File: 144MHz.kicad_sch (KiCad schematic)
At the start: 45 parts, among them J4 BWSMA-KWE-Z001, U5 GRF5604, U6 SKYA21003

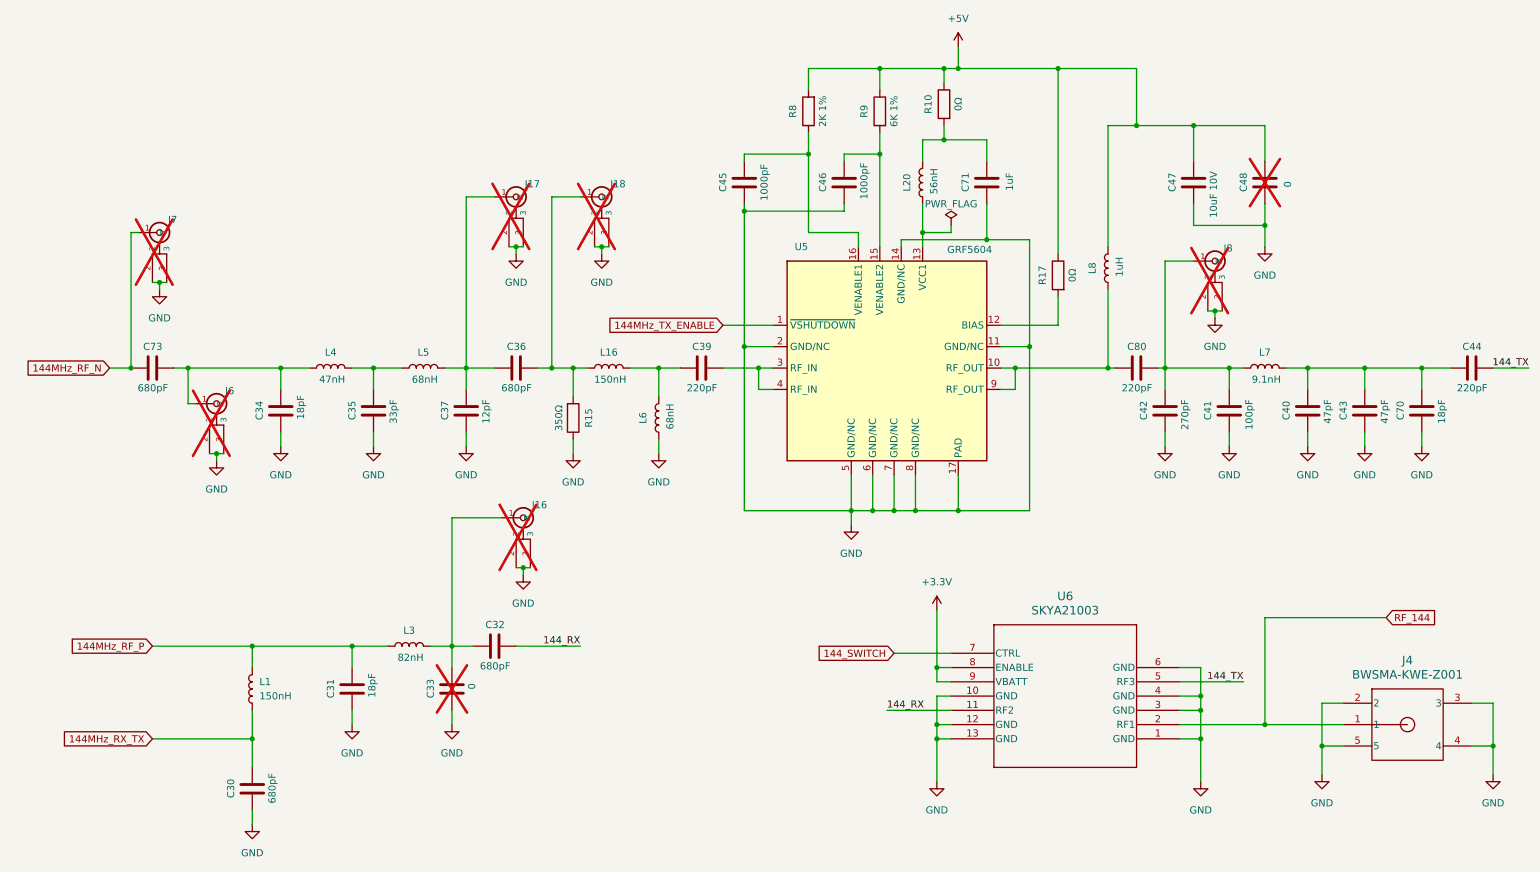
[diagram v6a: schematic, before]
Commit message: Reduce hole sizes and add more holes on PA
Meet spec requirements.

Signed-off-by: Corey Minyard <corey@minyard.net>
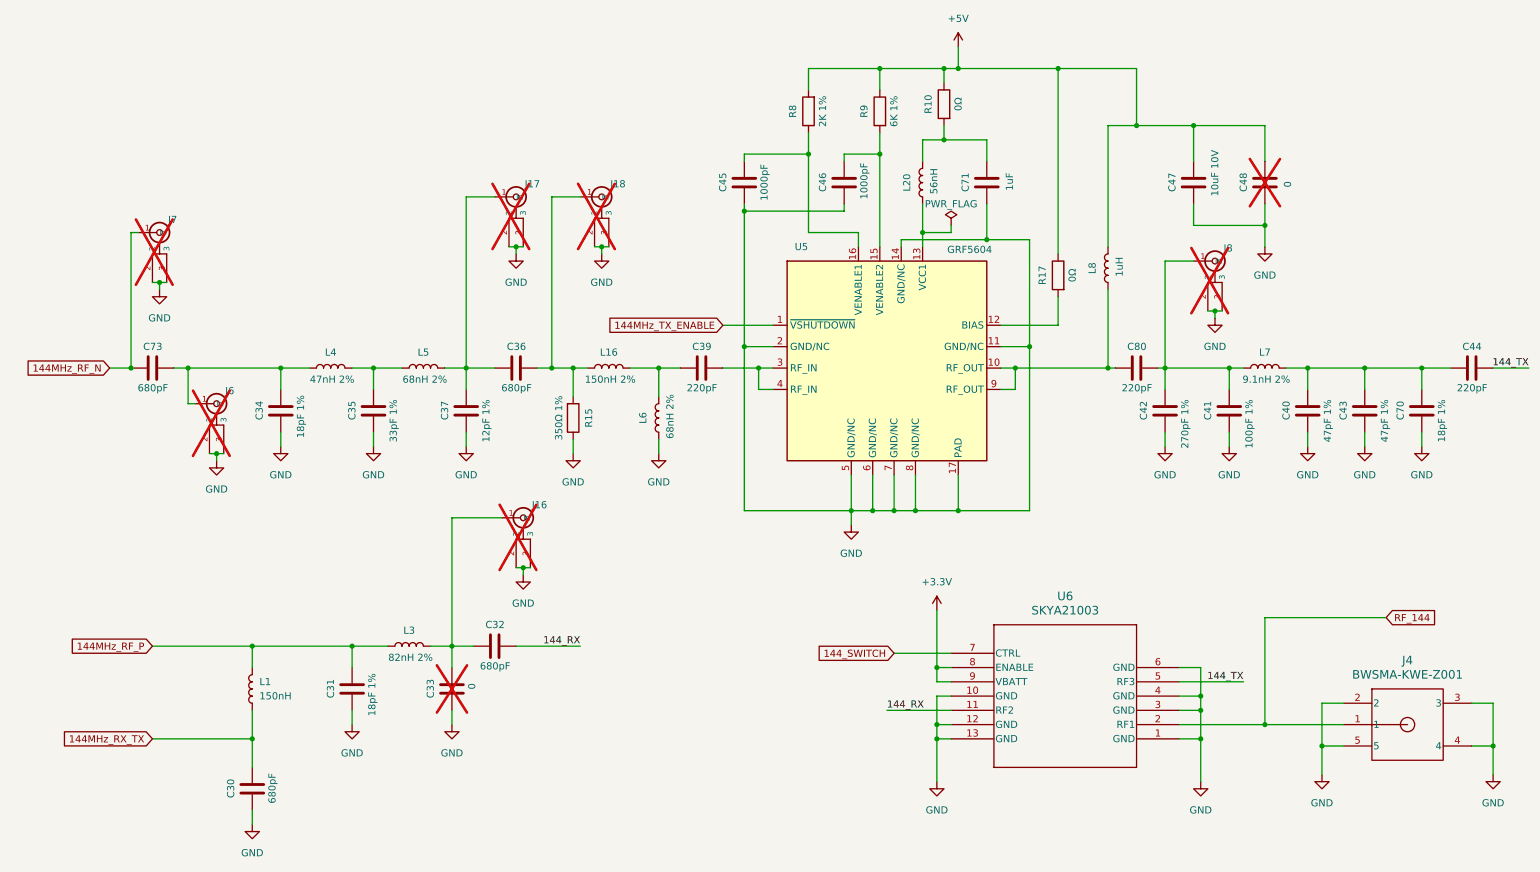
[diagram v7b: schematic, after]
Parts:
- C31, C34, C70: value 18pF -> 18pF 1%
- C35: value 33pF -> 33pF 1%
- C37: value 12pF -> 12pF 1%
- C40, C43: value 47pF -> 47pF 1%
- C41: value 100pF -> 100pF 1%
- C42: value 270pF -> 270pF 1%
- L16: value 150nH -> 150nH 2%
- L3: value 82nH -> 82nH 2%
- L4: value 47nH -> 47nH 2%
- L5, L6: value 68nH -> 68nH 2%
- L7: value 9.1nH -> 9.1nH 2%
- R15: value 350Ω -> 350Ω 1%
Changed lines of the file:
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@@
 			)
 		)
-		(property "Value" "68nH"
+		(property "Value" "68nH 2%"
 			(at 85.344 80.772 90)
 			(effects
@@
 		)
 		(property "Value" "10uF 10V"
-			(at 225.806 43.688 90)
+			(at 226.06 39.878 90)
 			(effects
 				(font
@@
 			)
 		)
-		(property "Value" "150nH"
+		(property "Value" "150nH 2%"
 			(at 118.364 80.772 90)
 			(effects
@@
 			)
 		)
-		(property "Value" "270pF"
+		(property "Value" "270pF 1%"
 			(at 220.726 84.328 90)
 			(effects
@@
 			)
 		)
-		(property "Value" "9.1nH"
+		(property "Value" "9.1nH 2%"
 			(at 235.204 80.772 90)
 			(effects
@@
 			)
 		)
-		(property "Value" "18pF"
+		(property "Value" "18pF 1%"
 			(at 63.246 83.566 90)
 			(effects
@@
 			)
 		)
-		(property "Value" "12pF"
+		(property "Value" "12pF 1%"
 			(at 96.266 84.328 90)
 			(effects
@@
 			)
 		)
-		(property "Value" "68nH"
+		(property "Value" "68nH 2%"
 			(at 129.032 87.376 90)
 			(effects
@@
 			)
 		)
-		(property "Value" "47pF"
+		(property "Value" "47pF 1%"
 			(at 256.286 84.328 90)
 			(effects
@@
 			)
 		)
-		(property "Value" "82nH"
+		(property "Value" "82nH 2%"
 			(at 82.804 130.302 90)
 			(effects
@@
 			)
 		)
-		(property "Value" "33pF"
+		(property "Value" "33pF 1%"
 			(at 79.756 84.328 90)
 			(effects
@@
 			)
 		)
-		(property "Value" "47nH"
+		(property "Value" "47nH 2%"
 			(at 68.834 80.772 90)
 			(effects
@@
 			)
 		)
-		(property "Value" "47pF"
+		(property "Value" "47pF 1%"
 			(at 246.126 84.328 90)
 			(effects
@@
 			)
 		)
-		(property "Value" "100pF"
+		(property "Value" "100pF 1%"
 			(at 232.156 84.328 90)
 			(effects
@@
 			)
 		)
-		(property "Value" "18pF"
+		(property "Value" "18pF 1%"
 			(at 75.946 133.096 90)
 			(effects
@@
 			)
 		)
-		(property "Value" "18pF"
+		(property "Value" "18pF 1%"
 			(at 266.446 84.328 90)
 			(effects
@@
 			)
 		)
-		(property "Value" "350Ω"
+		(property "Value" "350Ω 1%"
 			(at 109.22 87.63 90)
 			(effects

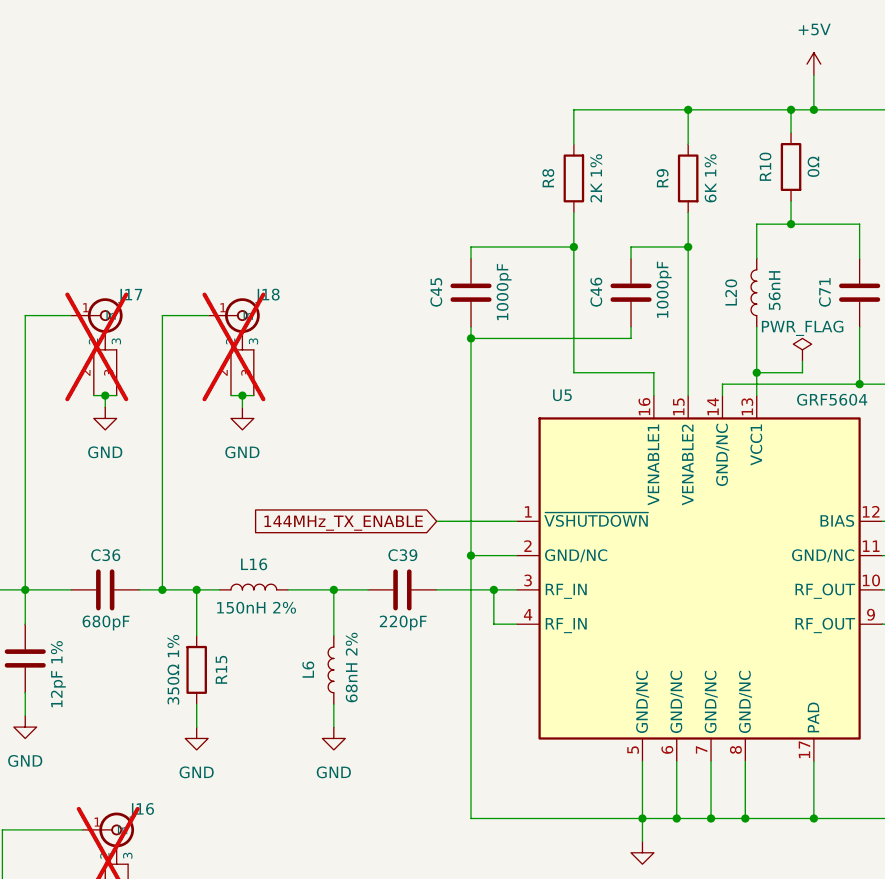
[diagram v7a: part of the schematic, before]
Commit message: Start working on BOM, fix supply indoctors
Signed-off-by: Corey Minyard <corey@minyard.net>
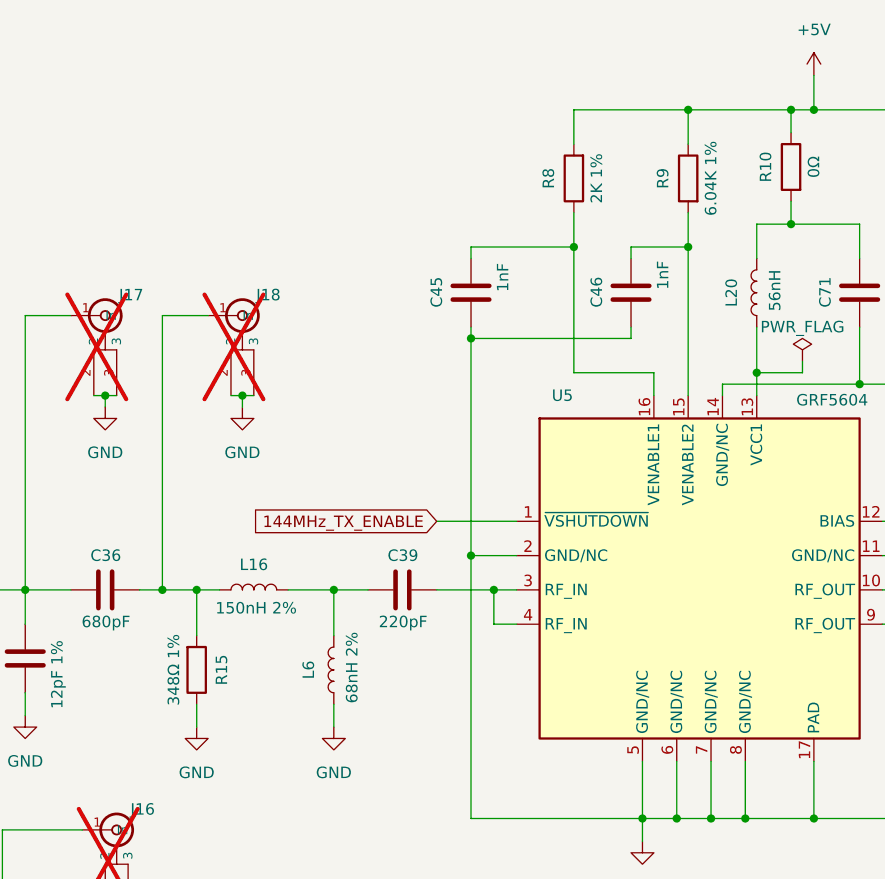
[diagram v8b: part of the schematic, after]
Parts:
- C45, C46: value 1000pF -> 1nF
- C47: footprint Capacitor_SMD:C_0805_2012Metric_Pad1.18x1.45mm_HandSolder -> Capacitor_SMD:C_1206_3216Metric_Pad1.33x1.80mm_HandSolder
- C71: footprint Capacitor_SMD:C_0402_1005Metric_Pad0.74x0.62mm_HandSolder -> Capacitor_SMD:C_0603_1608Metric_Pad1.08x0.95mm_HandSolder
- L8: footprint Inductor_SMD:L_1210_3225Metric_Pad1.42x2.65mm_HandSolder -> Inductor_SMD:L_1008_2520Metric_Pad1.43x2.20mm_HandSolder
- R15: value 350Ω 1% -> 348Ω 1%
- R9: value 6K 1% -> 6.04K 1%
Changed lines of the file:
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@@
 			)
 		)
-		(property "Value" "6K 1%"
+		(property "Value" "6.04K 1%"
 			(at 168.91 33.02 90)
 			(effects
@@
 			)
 		)
-		(property "Footprint" "Capacitor_SMD:C_0805_2012Metric_Pad1.18x1.45mm_HandSolder"
+		(property "Footprint" "Capacitor_SMD:C_1206_3216Metric_Pad1.33x1.80mm_HandSolder"
 			(at 221.2848 41.91 0)
 			(effects
@@
 			)
 		)
-		(property "Footprint" "Inductor_SMD:L_1210_3225Metric_Pad1.42x2.65mm_HandSolder"
+		(property "Footprint" "Inductor_SMD:L_1008_2520Metric_Pad1.43x2.20mm_HandSolder"
 			(at 207.01 60.96 0)
 			(effects
@@
 			)
 		)
-		(property "Value" "1000pF"
+		(property "Value" "1nF"
 			(at 163.576 42.164 90)
 			(effects
@@
 			)
 		)
-		(property "Value" "350Ω 1%"
+		(property "Value" "348Ω 1%"
 			(at 109.22 87.63 90)
 			(effects
@@
 			)
 		)
-		(property "Value" "1000pF"
+		(property "Value" "1nF"
 			(at 145.796 42.418 90)
 			(effects
@@
 			)
 		)
-		(property "Footprint" "Capacitor_SMD:C_0402_1005Metric_Pad0.74x0.62mm_HandSolder"
+		(property "Footprint" "Capacitor_SMD:C_0603_1608Metric_Pad1.08x0.95mm_HandSolder"
 			(at 184.4548 41.91 0)
 			(effects
